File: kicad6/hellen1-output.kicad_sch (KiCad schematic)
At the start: 56 parts

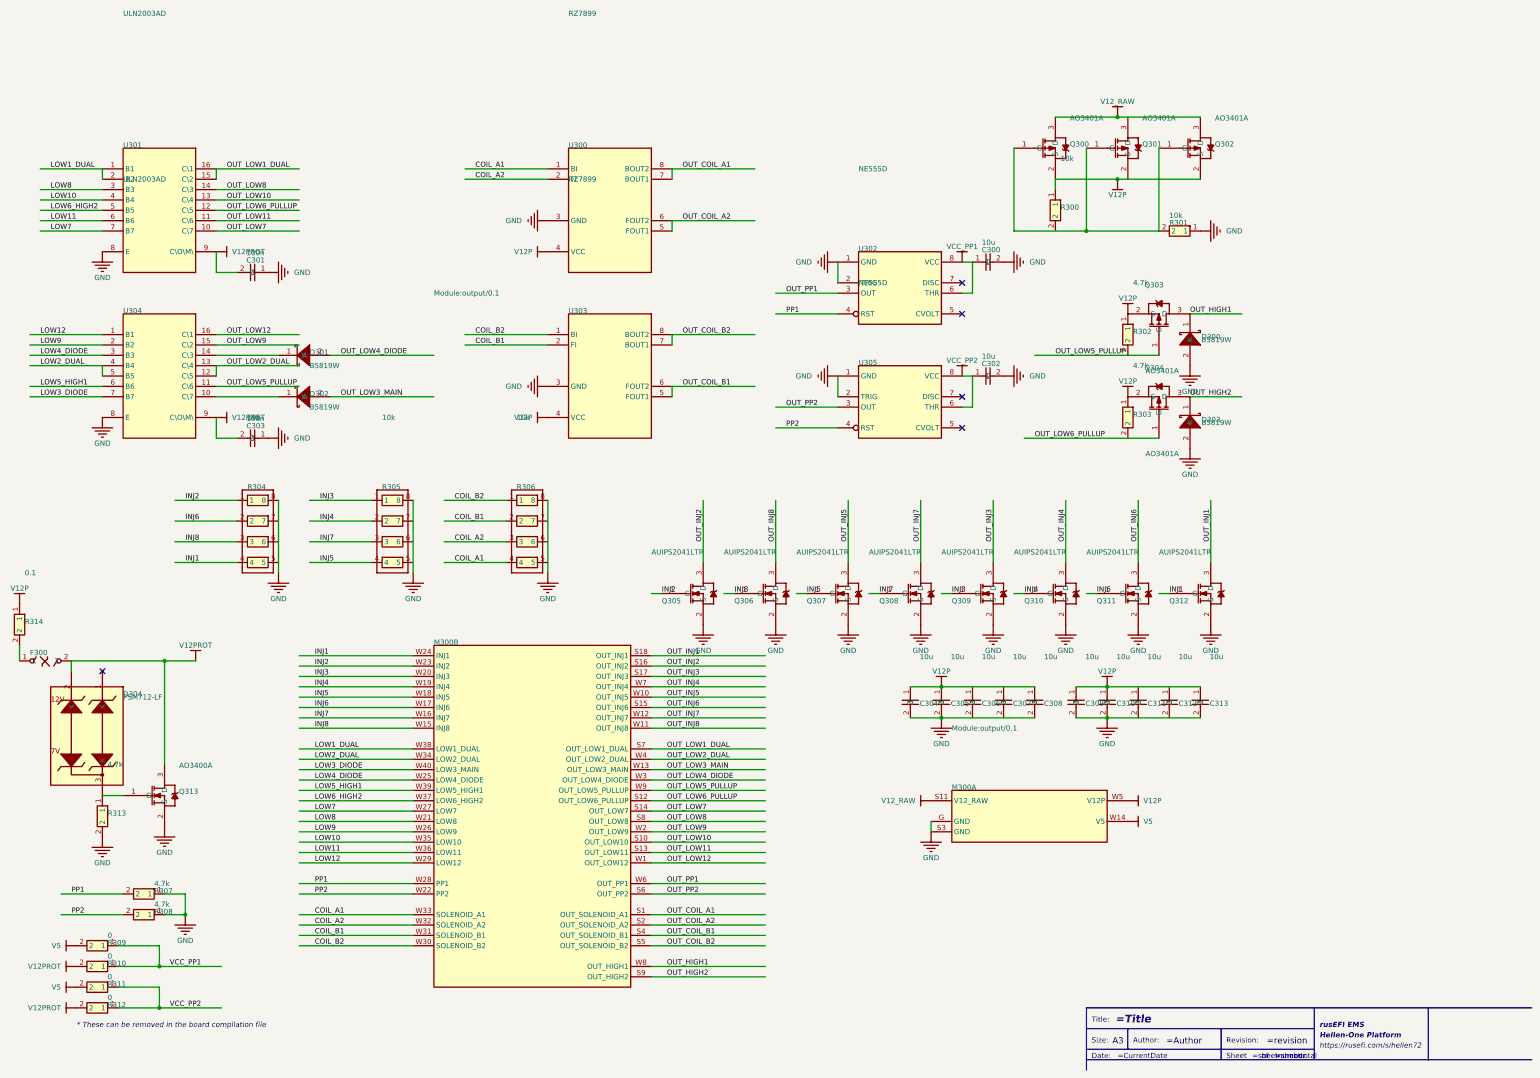
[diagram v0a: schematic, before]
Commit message: move kicad src files into a separate folder
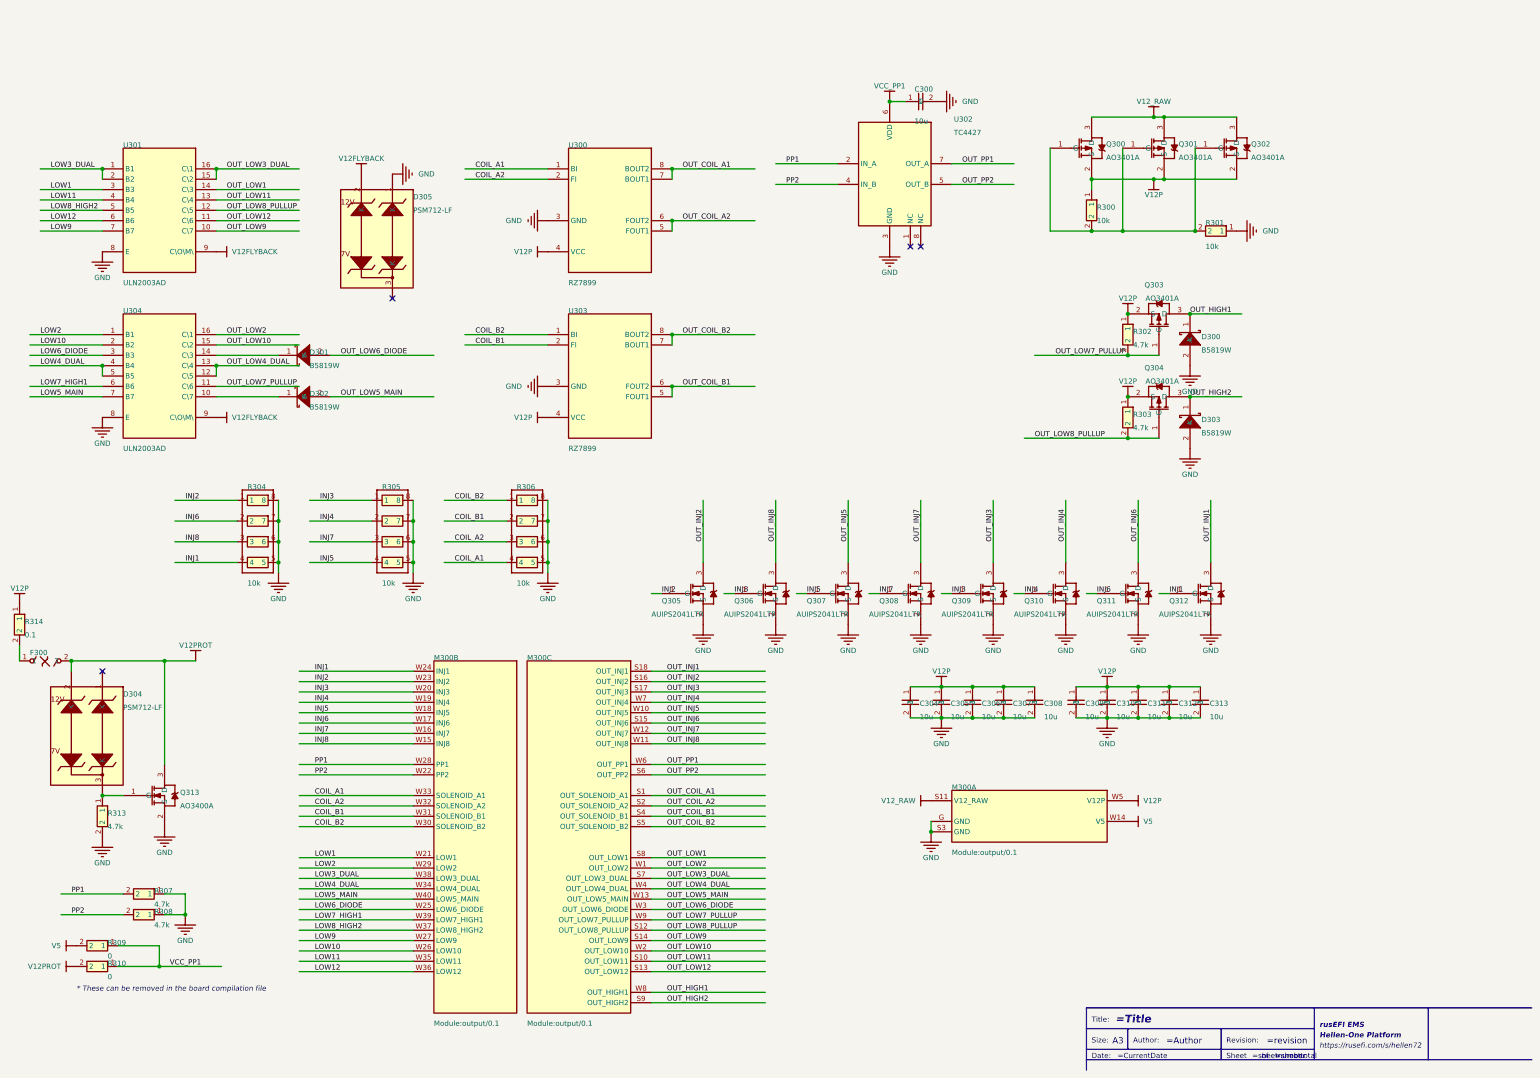
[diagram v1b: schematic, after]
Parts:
- removed C301, C303: ~, symbol hellen1-output-altium-import:3_Cap
- removed C302: ~, symbol hellen1-output-altium-import:1_Cap
- removed R311, R312: ~, symbol hellen1-output-altium-import:1_mirrored_Res
- removed U302, U305: ~, symbol hellen1-output-altium-import:0_NE555D
- added D305: PSM712-LF, symbol hellen1-output-altium-import:3_D TVS PSM712-12
- added unit 3 of M300
- added U302: TC4427, symbol hellen1-output-altium-import:0_TC4427
- C300, C304, C305, C306, C307, C308, C309, C310, C311, C312, C313: value ~ -> 10u; Comment 10u -> (none)
- D300, D301, D302, D303: value ~ -> B5819W; Comment B5819W -> (none)
- D304: value ~ -> PSM712-LF; Comment PSM712-LF -> (none)
- F300: value ~ -> SMD1206P050TF/24; Comment SMD1206P050TF/24 -> (none)
- M300: value ~ -> Module:output/0.1; Comment Module:output/0.1 -> (none)
- Q300, Q301, Q302, Q303, Q304: value ~ -> AO3401A; Comment AO3401A -> (none)
- Q305, Q306, Q307, Q308, Q309, Q310, Q311, Q312: value ~ -> AUIPS2041LTR; Comment AUIPS2041LTR -> (none)
- Q313: value ~ -> AO3400A; Comment AO3400A -> (none); Supplier Part Number 3 C20917 -> C344010
- R300, R301, R304, R305, R306: value ~ -> 10k; Comment 10k -> (none)
- R302, R303, R307, R308, R313: value ~ -> 4.7k; Comment 4.7k -> (none)
- R309, R310: value ~ -> 0; Comment 0 -> (none)
- R314: value ~ -> 0.1; Comment 0.1 -> (none)
- U300, U303: value ~ -> RZ7899; Comment RZ7899 -> (none)
- U301, U304: value ~ -> ULN2003AD; Comment ULN2003AD -> (none)
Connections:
- net LOW7 is gone; now on net LOW9: M300.W27 (LOW9), U301.7 (B7)
- net GND: now also C306.2, C307.2, C311.2, C312.2, R304.5, R304.6, R304.7, R305.5, R305.6, R305.7, R306.5, R306.6, R306.7, D305.1 (K), U302.3 (GND)
- net LOW10: now also M300.W26 (LOW10), U304.2 (B2); no longer M300.W35 (LOW10), U301.4 (B4)
- net LOW11: now also M300.W35 (LOW11), U301.4 (B4); no longer M300.W36 (LOW11), U301.6 (B6)
- net LOW12: now also M300.W36 (LOW12), U301.6 (B6); no longer M300.W29 (LOW12), U304.1 (B1)
- net LOW9: no longer M300.W26 (LOW9), U304.2 (B2)
- net OUT_COIL_A1: now also M300.S1 (OUT_SOLENOID_A1); no longer M300.S1 (OUT_SOLENOID_A1)
- net OUT_COIL_A2: now also M300.S2 (OUT_SOLENOID_A2); no longer M300.S2 (OUT_SOLENOID_A2)
- net OUT_COIL_B1: now also M300.S4 (OUT_SOLENOID_B1); no longer M300.S4 (OUT_SOLENOID_B1)
- net OUT_COIL_B2: now also M300.S5 (OUT_SOLENOID_B2); no longer M300.S5 (OUT_SOLENOID_B2)
- net OUT_HIGH1: now also M300.W8 (OUT_HIGH1); no longer M300.W8 (OUT_HIGH1)
- net OUT_HIGH2: now also M300.S9 (OUT_HIGH2); no longer M300.S9 (OUT_HIGH2)
- net OUT_INJ1: now also M300.S18 (OUT_INJ1); no longer M300.S18 (OUT_INJ1)
- net OUT_INJ2: now also M300.S16 (OUT_INJ2); no longer M300.S16 (OUT_INJ2)
- net OUT_INJ3: now also M300.S17 (OUT_INJ3); no longer M300.S17 (OUT_INJ3)
- net OUT_INJ4: now also M300.W7 (OUT_INJ4); no longer M300.W7 (OUT_INJ4)
- net OUT_INJ5: now also M300.W10 (OUT_INJ5); no longer M300.W10 (OUT_INJ5)
- net OUT_INJ6: now also M300.S15 (OUT_INJ6); no longer M300.S15 (OUT_INJ6)
- net OUT_INJ7: now also M300.W12 (OUT_INJ7); no longer M300.W12 (OUT_INJ7)
- net OUT_INJ8: now also M300.W11 (OUT_INJ8); no longer M300.W11 (OUT_INJ8)
- net OUT_LOW10: now also U304.15 (C\2), M300.W2 (OUT_LOW10); no longer M300.S10 (OUT_LOW10), U301.13 (C\4)
- net OUT_LOW11: now also U301.13 (C\4), M300.S10 (OUT_LOW11); no longer M300.S13 (OUT_LOW11), U301.11 (C\6)
- net OUT_LOW12: now also U301.11 (C\6), M300.S13 (OUT_LOW12); no longer M300.W1 (OUT_LOW12), U304.16 (C\1)
- net OUT_LOW9: now also U301.10 (C\7), M300.S14 (OUT_LOW9); no longer M300.W2 (OUT_LOW9), U304.15 (C\2)
- net OUT_PP1: now also M300.W6 (OUT_PP1), U302.7 (OUT_A); no longer M300.W6 (OUT_PP1)
- net OUT_PP2: now also M300.S6 (OUT_PP2), U302.5 (OUT_B); no longer M300.S6 (OUT_PP2)
- net PP1: now also U302.2 (IN_A)
- net PP2: now also U302.4 (IN_B)
- net V12P: now also C306.1, C307.1, C311.1, C312.1, Q301.2 (S)
- net V12PROT: no longer U301.9 (C\O\M\), U304.9 (C\O\M\)
- net V12_RAW: now also Q301.3 (D)
- net VCC_PP1: now also U302.6 (VDD)
- net at Q300.1 (G), Q301.1 (G), Q302.1 (G)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: now also R300.2
- net OUT_LOW8_PULLUP: now reaches R303.2
- net OUT_LOW8_PULLUP: now also Q304.1 (G), U301.12 (C\5), M300.S12 (OUT_LOW8_PULLUP)
- net OUT_LOW7_PULLUP: now reaches R302.2
- net OUT_LOW7_PULLUP: now also Q303.1 (G), U304.11 (C\6), M300.W9 (OUT_LOW7_PULLUP)
- net LOW1_DUAL renamed LOW3_DUAL
- net LOW2_DUAL renamed LOW4_DUAL
- net LOW3_DIODE renamed LOW5_MAIN
- net LOW4_DIODE renamed LOW6_DIODE
- net LOW5_HIGH1 renamed LOW7_HIGH1
- net LOW6_HIGH2 renamed LOW8_HIGH2
- net LOW8 renamed LOW1
- net OUT_LOW1_DUAL renamed OUT_LOW3_DUAL
- net OUT_LOW3_DUAL: now also M300.S7 (OUT_LOW3_DUAL); no longer M300.S7 (OUT_LOW1_DUAL)
- net OUT_LOW2_DUAL renamed OUT_LOW4_DUAL
- net OUT_LOW4_DUAL: now also M300.W4 (OUT_LOW4_DUAL); no longer M300.W4 (OUT_LOW2_DUAL)
- net OUT_LOW3_MAIN renamed OUT_LOW5_MAIN
- net OUT_LOW5_MAIN: now also M300.W13 (OUT_LOW5_MAIN); no longer M300.W13 (OUT_LOW3_MAIN)
- net OUT_LOW4_DIODE renamed OUT_LOW6_DIODE
- net OUT_LOW6_DIODE: now also M300.W3 (OUT_LOW6_DIODE); no longer M300.W3 (OUT_LOW4_DIODE)
- removed net OUT_LOW5_PULLUP: M300.W9 (OUT_LOW5_PULLUP), Q303.1 (G), U304.11 (C\6)
- removed net OUT_LOW6_PULLUP: M300.S12 (OUT_LOW6_PULLUP), Q304.1 (G), U301.12 (C\5)
- removed net OUT_LOW7: M300.S14 (OUT_LOW7), U301.10 (C\7)
- net OUT_LOW8 renamed OUT_LOW1
- net OUT_LOW1: now also M300.S8 (OUT_LOW1); no longer M300.S8 (OUT_LOW8)
- new net LOW2: M300.W29 (LOW2), U304.1 (B1)
- new net OUT_LOW2: M300.W1 (OUT_LOW2), U304.16 (C\1)
- new net V12FLYBACK: D305.2 (K), U301.9 (C\O\M\), U304.9 (C\O\M\)
- no-connect marks 5 -> 4
